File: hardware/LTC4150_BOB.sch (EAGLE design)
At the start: 23 parts, among them U1 LTC4150

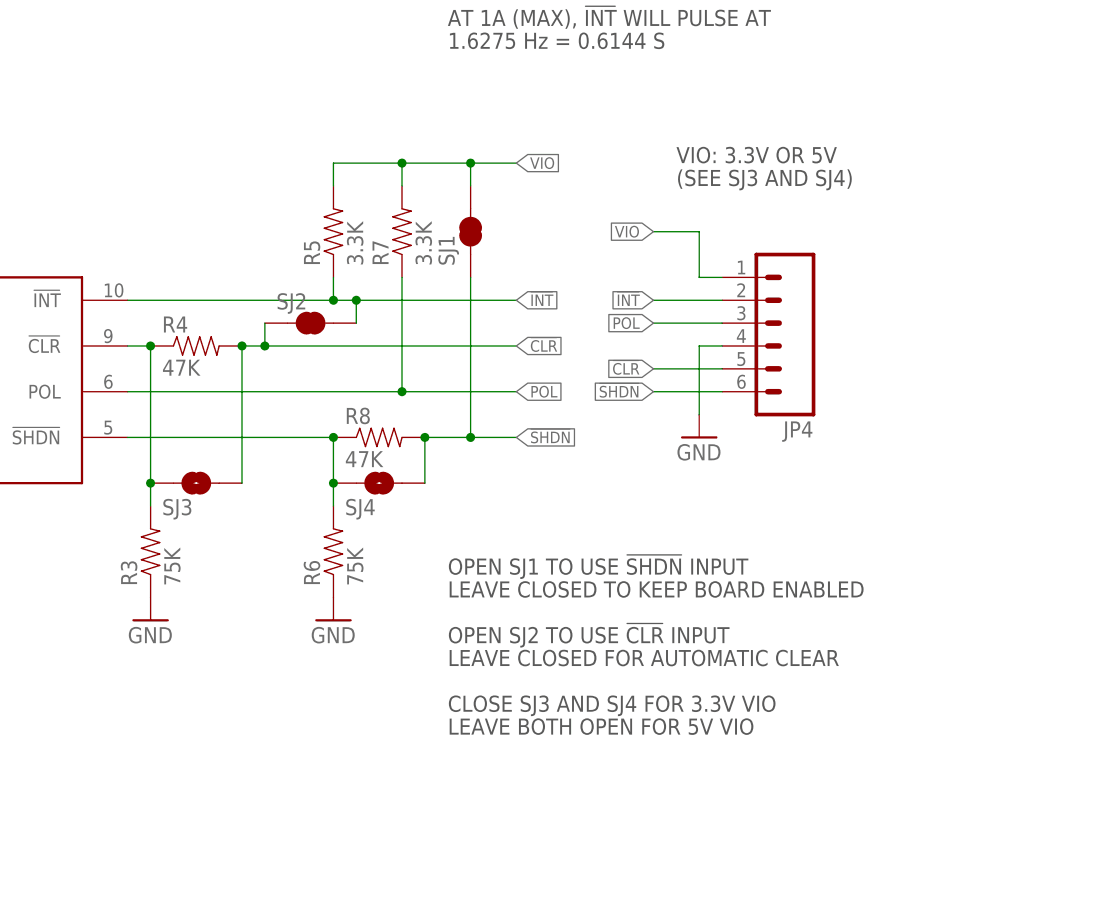
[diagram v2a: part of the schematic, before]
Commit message: Replaced solder jumper with pullup resistor
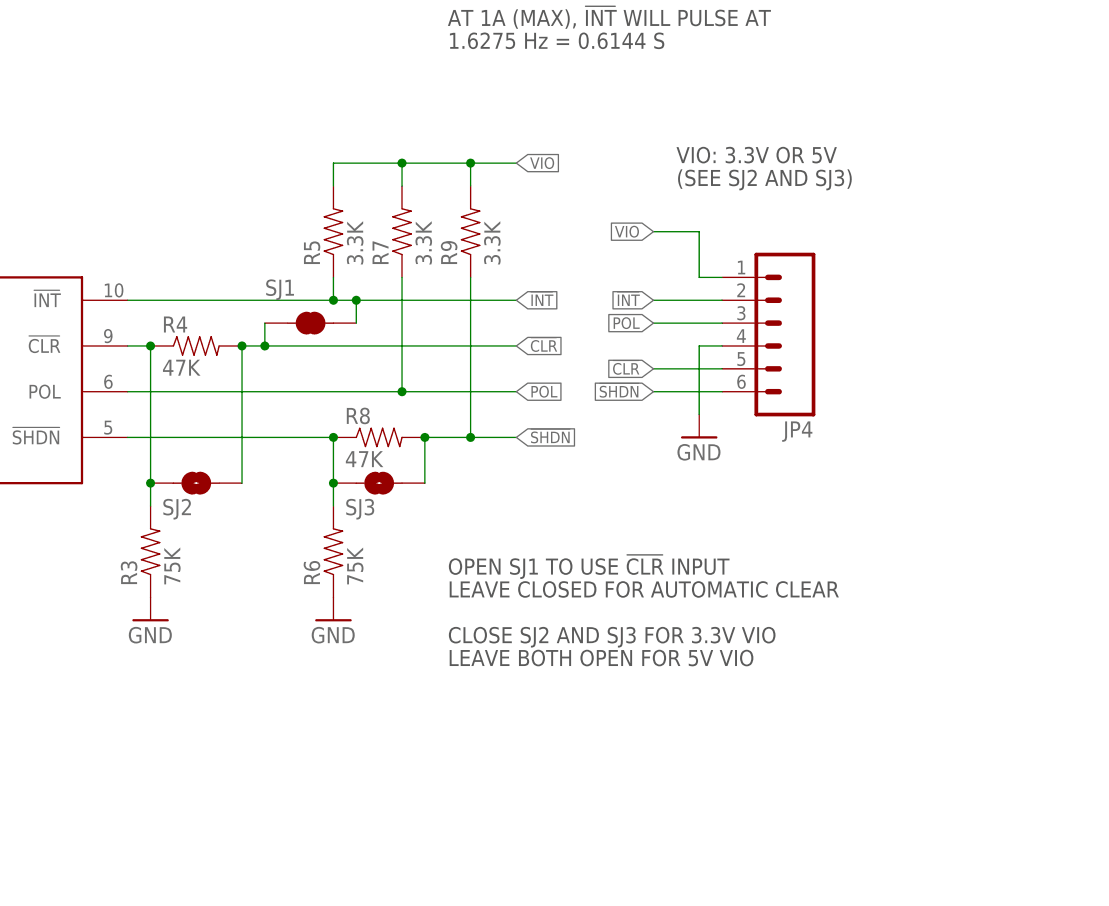
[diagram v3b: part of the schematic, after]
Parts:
- removed SJ4: SOLDERJUMPERNO, SparkFun-Passives:SOLDERJUMPERNO
- added R9: 3.3K, SparkFun-Passives:RESISTOR0603-RES
- SJ2: value SOLDERJUMPERNC -> SOLDERJUMPERNO; device SparkFun-Passives:SOLDERJUMPERNC -> SparkFun-Passives:SOLDERJUMPERNO
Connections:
- net !CLR!: now also SJ1.1, SJ2.2; no longer SJ2.1, SJ3.2
- net !INT!: now also SJ1.2; no longer SJ2.2
- net !SHDN!: now also R9.1, SJ3.2; no longer SJ1.2, SJ4.2
- net N$1: now also SJ2.1; no longer SJ3.1
- net N$9: now also SJ3.1; no longer SJ4.1
- net VIO: now also R9.2; no longer SJ1.1
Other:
- note added: "(SEE SJ2 AND SJ3)"
- note added: "CLOSE SJ2 AND SJ3 FOR 3.3V VIO"
- note added: "OPEN SJ1 TO USE !CLR! INPUT"
- note removed: "(SEE SJ3 AND SJ4)"
- note removed: "CLOSE SJ3 AND SJ4 FOR 3.3V VIO"
- note removed: "LEAVE CLOSED TO KEEP BOARD ENABLED"
- note removed: "OPEN SJ1 TO USE !SHDN! INPUT"
- note removed: "OPEN SJ2 TO USE !CLR! INPUT"
- moved on the sheet: SJ1, SJ2, SJ3
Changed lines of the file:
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@@
 <part name="LOGO3" library="SparkFun-Aesthetics" deviceset="LOGO-SFE" device="SK"/>
 <part name="LOGO1" library="SparkFun-Aesthetics" deviceset="OSHW-LOGO" device="S"/>
+<part name="SJ2" library="SparkFun-Passives" deviceset="SOLDERJUMPER" device="NO" value=""/>
+<part name="LOGO2" library="SparkFun-Aesthetics" deviceset="LOGO-SFE" device="NW2"/>
+<part name="SJ1" library="SparkFun-Passives" deviceset="SOLDERJUMPER" device="NC" value=""/>
+<part name="R2" library="SparkFun-Passives" deviceset="RESISTOR" device="AXIAL-0.3" value="DNP"/>
 <part name="SJ3" library="SparkFun-Passives" deviceset="SOLDERJUMPER" device="NO" value=""/>
-<part name="SJ1" library="SparkFun-Passives" deviceset="SOLDERJUMPER" device="NC" value=""/>
-<part name="LOGO2" library="SparkFun-Aesthetics" deviceset="LOGO-SFE" device="NW2"/>
-<part name="SJ2" library="SparkFun-Passives" deviceset="SOLDERJUMPER" device="NC" value=""/>
-<part name="R2" library="SparkFun-Passives" deviceset="RESISTOR" device="AXIAL-0.3" value="DNP"/>
-<part name="SJ4" library="SparkFun-Passives" deviceset="SOLDERJUMPER" device="NO" value=""/>
+<part name="R9" library="SparkFun-Passives" deviceset="RESISTOR" device="0603-RES" value="3.3K"/>
 </parts>
 <sheets>
@@
 <text x="172.72" y="7.62" size="2.54" layer="94">M Grusin</text>
 <text x="238.76" y="7.62" size="2.54" layer="94">10</text>
-<text x="165.1" y="66.04" size="1.778" layer="97">CLOSE SJ3 AND SJ4 FOR 3.3V VIO</text>
-<text x="165.1" y="81.28" size="1.778" layer="97">OPEN SJ1 TO USE !SHDN! INPUT</text>
+<text x="165.1" y="73.66" size="1.778" layer="97">CLOSE SJ2 AND SJ3 FOR 3.3V VIO</text>
 <text x="45.72" y="149.86" size="1.778" layer="97">CURRENT SENSE TERMINALS:</text>
-<text x="165.1" y="63.5" size="1.778" layer="97">LEAVE BOTH OPEN FOR 5V VIO</text>
+<text x="165.1" y="71.12" size="1.778" layer="97">LEAVE BOTH OPEN FOR 5V VIO</text>
 <text x="165.1" y="142.24" size="1.778" layer="97">AT 1A (MAX), !INT! WILL PULSE AT</text>
 <text x="165.1" y="139.7" size="1.778" layer="97">1.6275 Hz = 0.6144 S</text>
 <text x="165.1" y="149.86" size="1.778" layer="97">1 !INT! = 0.0001707 Ah</text>
 <text x="165.1" y="147.32" size="1.778" layer="97">5859 !INT!S = 1 Ah</text>
-<text x="165.1" y="73.66" size="1.778" layer="97">OPEN SJ2 TO USE !CLR! INPUT</text>
+<text x="165.1" y="81.28" size="1.778" layer="97">OPEN SJ1 TO USE !CLR! INPUT</text>
 <rectangle x1="149.098" y1="108.712" x2="150.622" y2="109.728" layer="94"/>
-<rectangle x1="167.132" y1="118.364" x2="168.148" y2="120.142" layer="94"/>
 <text x="45.72" y="142.24" size="1.778" layer="97">1.0A MAX (FOR 0.05 OHM SENSE RESISTOR)</text>
 <text x="190.5" y="127" size="1.778" layer="97">VIO: 3.3V OR 5V</text>
-<text x="190.5" y="124.46" size="1.778" layer="97">(SEE SJ3 AND SJ4)</text>
-<text x="165.1" y="78.74" size="1.778" layer="97">LEAVE CLOSED TO KEEP BOARD ENABLED</text>
-<text x="165.1" y="71.12" size="1.778" layer="97">LEAVE CLOSED FOR AUTOMATIC CLEAR</text>
+<text x="190.5" y="124.46" size="1.778" layer="97">(SEE SJ2 AND SJ3)</text>
+<text x="165.1" y="78.74" size="1.778" layer="97">LEAVE CLOSED FOR AUTOMATIC CLEAR</text>
 <text x="45.72" y="144.78" size="1.778" layer="97">8.5V MAX</text>
 <text x="45.72" y="137.16" size="1.778" layer="97">POL SIGNAL:</text>
@@
 <instance part="LOGO3" gate="G$1" x="139.7" y="2.54"/>
 <instance part="LOGO1" gate="G$1" x="121.92" y="12.7"/>
-<instance part="SJ3" gate="1" x="137.16" y="91.44" smashed="yes" rot="MR180">
+<instance part="SJ2" gate="1" x="137.16" y="91.44" smashed="yes" rot="MR180">
 <attribute name="NAME" x="133.35" y="89.662" size="1.778" layer="95" rot="MR180"/>
 <attribute name="VALUE" x="134.62" y="96.52" size="1.778" layer="96" rot="MR180"/>
 </instance>
-<instance part="SJ1" gate="1" x="167.64" y="119.38" smashed="yes" rot="MR270">
-<attribute name="NAME" x="165.862" y="115.57" size="1.778" layer="95" rot="R90"/>
-</instance>
 <instance part="LOGO2" gate="G$1" x="139.7" y="10.16"/>
-<instance part="SJ2" gate="1" x="149.86" y="109.22" smashed="yes" rot="MR180">
-<attribute name="NAME" x="146.05" y="112.522" size="1.778" layer="95" rot="MR180"/>
+<instance part="SJ1" gate="1" x="149.86" y="109.22" smashed="yes" rot="MR180">
+<attribute name="NAME" x="144.78" y="114.046" size="1.778" layer="95" rot="MR180"/>
 <attribute name="VALUE" x="147.32" y="114.3" size="1.778" layer="96" rot="MR180"/>
 </instance>
 <instance part="R2" gate="G$1" x="71.12" y="114.3"/>
-<instance part="SJ4" gate="1" x="157.48" y="91.44" smashed="yes" rot="MR180">
+<instance part="SJ3" gate="1" x="157.48" y="91.44" smashed="yes" rot="MR180">
 <attribute name="NAME" x="153.67" y="89.662" size="1.778" layer="95" rot="MR180"/>
 <attribute name="VALUE" x="154.94" y="96.52" size="1.778" layer="96" rot="MR180"/>
 </instance>
+<instance part="R9" gate="G$1" x="167.64" y="119.38" rot="R90"/>
 </instances>
 <busses>
@@
 <junction x="152.4" y="111.76"/>
 <label x="172.72" y="111.76" size="1.27" layer="95" xref="yes"/>
-<pinref part="SJ2" gate="1" pin="2"/>
+<pinref part="SJ1" gate="1" pin="2"/>
 <wire x1="154.94" y1="109.22" x2="154.94" y2="111.76" width="0.1524" layer="91"/>
 <junction x="154.94" y="111.76"/>
@@
 <junction x="152.4" y="96.52"/>
 <pinref part="R8" gate="G$1" pin="1"/>
-<pinref part="SJ4" gate="1" pin="1"/>
+<pinref part="SJ3" gate="1" pin="1"/>
 <wire x1="152.4" y1="88.9" x2="152.4" y2="91.44" width="0.1524" layer="91"/>
 <junction x="152.4" y="91.44"/>
@@
 <wire x1="162.56" y1="96.52" x2="167.64" y2="96.52" width="0.1524" layer="91"/>
 <label x="172.72" y="96.52" size="1.27" layer="95" xref="yes"/>
-<pinref part="SJ1" gate="1" pin="2"/>
 <wire x1="167.64" y1="96.52" x2="172.72" y2="96.52" width="0.1524" layer="91"/>
 <wire x1="167.64" y1="114.3" x2="167.64" y2="96.52" width="0.1524" layer="91"/>
 <junction x="167.64" y="96.52"/>
-<pinref part="SJ4" gate="1" pin="2"/>
+<pinref part="SJ3" gate="1" pin="2"/>
 <wire x1="162.56" y1="91.44" x2="162.56" y2="96.52" width="0.1524" layer="91"/>
 <junction x="162.56" y="96.52"/>
+<pinref part="R9" gate="G$1" pin="1"/>
 </segment>
 <segment>
@@
 <junction x="160.02" y="127"/>
 <label x="172.72" y="127" size="1.27" layer="95" xref="yes"/>
-<pinref part="SJ1" gate="1" pin="1"/>
 <wire x1="167.64" y1="124.46" x2="167.64" y2="127" width="0.1524" layer="91"/>
 <junction x="167.64" y="127"/>
+<pinref part="R9" gate="G$1" pin="2"/>
 </segment>
 <segment>
@@
 <net name="!CLR!" class="0">
 <segment>
-<pinref part="SJ3" gate="1" pin="2"/>
+<pinref part="SJ2" gate="1" pin="2"/>
 <pinref part="R4" gate="G$1" pin="2"/>
 <junction x="142.24" y="106.68"/>
-<pinref part="SJ2" gate="1" pin="1"/>
+<pinref part="SJ1" gate="1" pin="1"/>
 <wire x1="142.24" y1="106.68" x2="142.24" y2="91.44" width="0.1524" layer="91"/>
 <wire x1="142.24" y1="106.68" x2="144.78" y2="106.68" width="0.1524" layer="91"/>
@@
 <segment>
 <pinref part="R3" gate="G$1" pin="2"/>
-<pinref part="SJ3" gate="1" pin="1"/>
+<pinref part="SJ2" gate="1" pin="1"/>
 <wire x1="132.08" y1="88.9" x2="132.08" y2="91.44" width="0.1524" layer="91"/>
 <pinref part="R4" gate="G$1" pin="1"/>

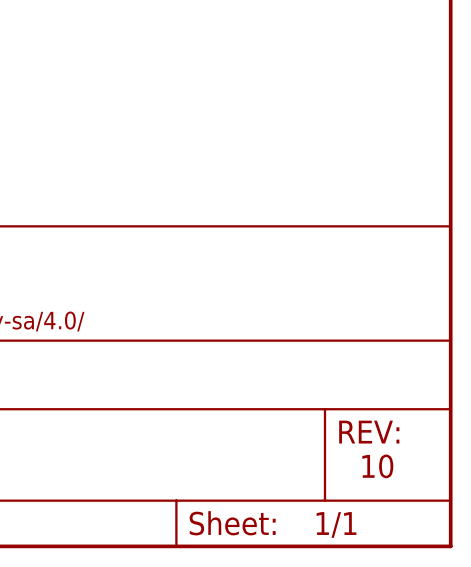
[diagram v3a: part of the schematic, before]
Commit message: added board fiducials
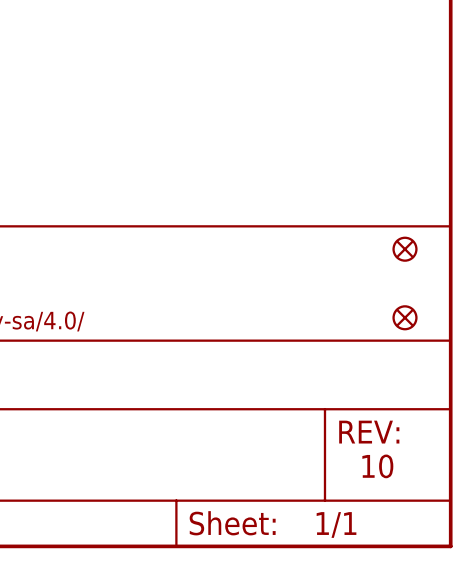
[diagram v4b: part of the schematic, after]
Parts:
- added FID1, FID2: FIDUCIAL1X2, SparkFun-Aesthetics:FIDUCIAL1X2
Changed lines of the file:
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@@
 <part name="SJ3" library="SparkFun-Passives" deviceset="SOLDERJUMPER" device="NO" value=""/>
 <part name="R9" library="SparkFun-Passives" deviceset="RESISTOR" device="0603-RES" value="3.3K"/>
+<part name="FID1" library="SparkFun-Aesthetics" deviceset="FIDUCIAL" device="1X2"/>
+<part name="FID2" library="SparkFun-Aesthetics" deviceset="FIDUCIAL" device="1X2"/>
 </parts>
 <sheets>
@@
 </instance>
 <instance part="R9" gate="G$1" x="167.64" y="119.38" rot="R90"/>
+<instance part="FID1" gate="G$1" x="243.84" y="33.02"/>
+<instance part="FID2" gate="G$1" x="243.84" y="25.4"/>
 </instances>
 <busses>
